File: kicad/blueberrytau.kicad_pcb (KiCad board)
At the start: 4 copper layers, 49 x 35.9 mm, 56 parts, among them IC1 SN74LVC1G07DCK, J1 PMIC_DBG, J10 ANALOG IN, J11 EPS/ACS, J2 TE-2201778-1, J3 JTAG, J4 DEBUG, J5 VBUS, J6 GPIO, J7 USB1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

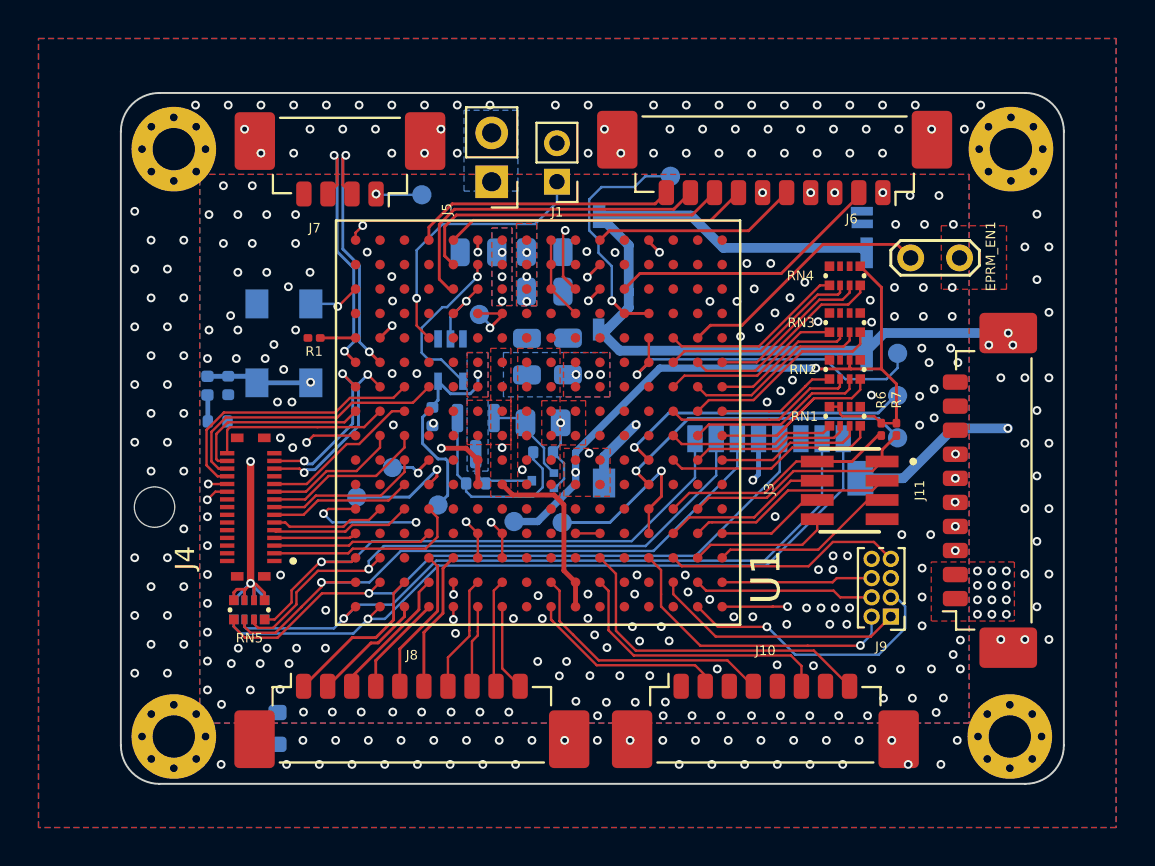
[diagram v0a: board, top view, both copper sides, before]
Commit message: Updated microSD slot shield net from earth to ground
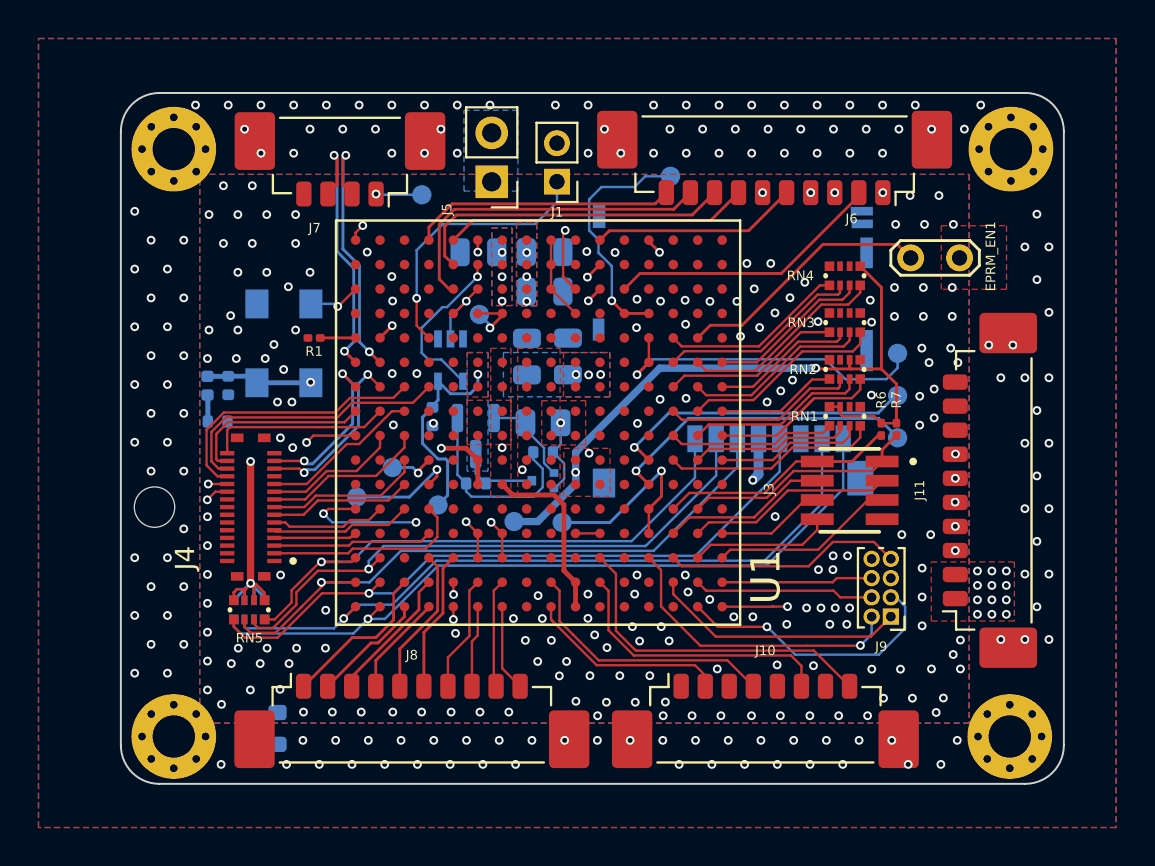
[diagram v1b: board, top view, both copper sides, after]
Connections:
- J2 pad 11: Earth -> GND
- J2 pad 12: Earth -> GND
- J2 pad 13: Earth -> GND
- J2 pad 14: Earth -> GND
- J2 pad 15: Earth -> GND
- J2 pad 16: Earth -> GND
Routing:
- net Earth: track 87.4 -> 0.00 mm, vias 146 -> 143
- net GND: vias 166 -> 176
